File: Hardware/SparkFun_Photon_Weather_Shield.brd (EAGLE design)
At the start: 66 x 35.6 mm, 44 parts, among them U1 3.3V MIC5219, U2 HTU21D, U3 MPL3115A2LGA8

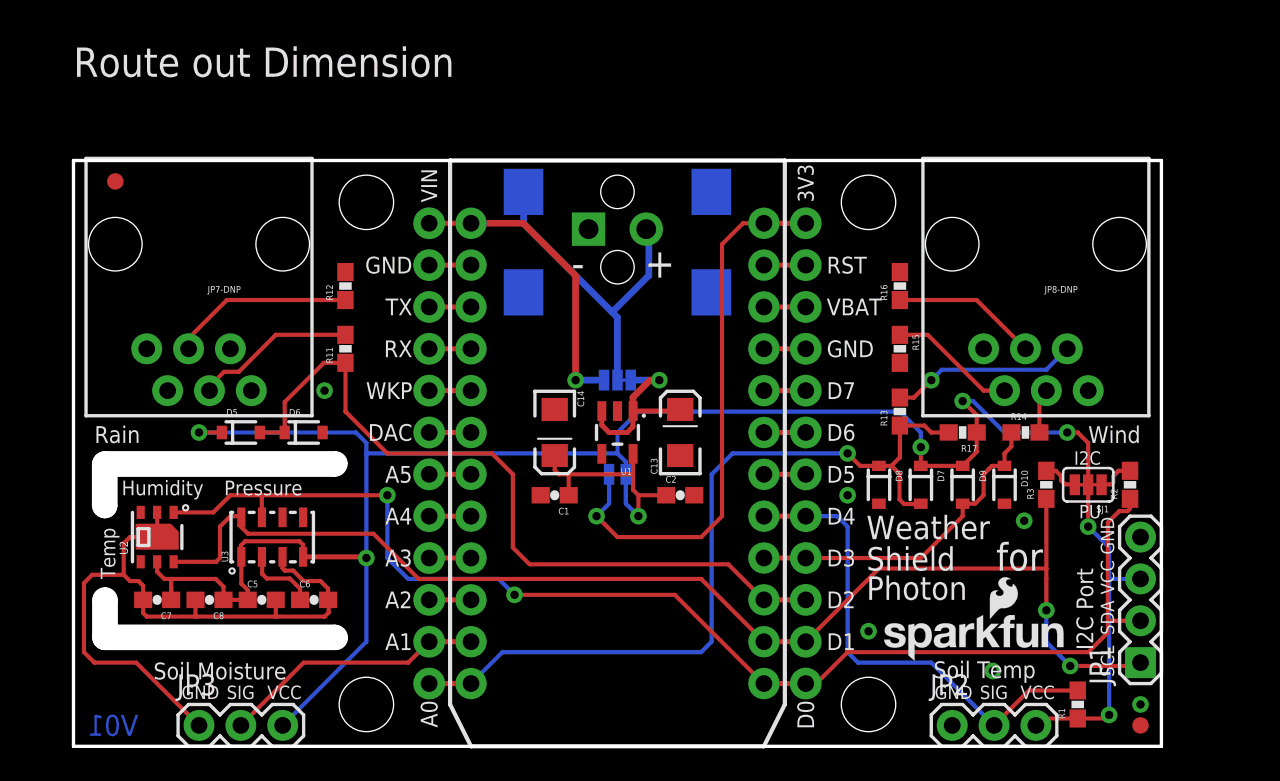
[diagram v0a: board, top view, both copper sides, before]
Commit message: Ready for Reds
Added USART port, changed soil moisture vcc to D5, minor silk and route
changes.
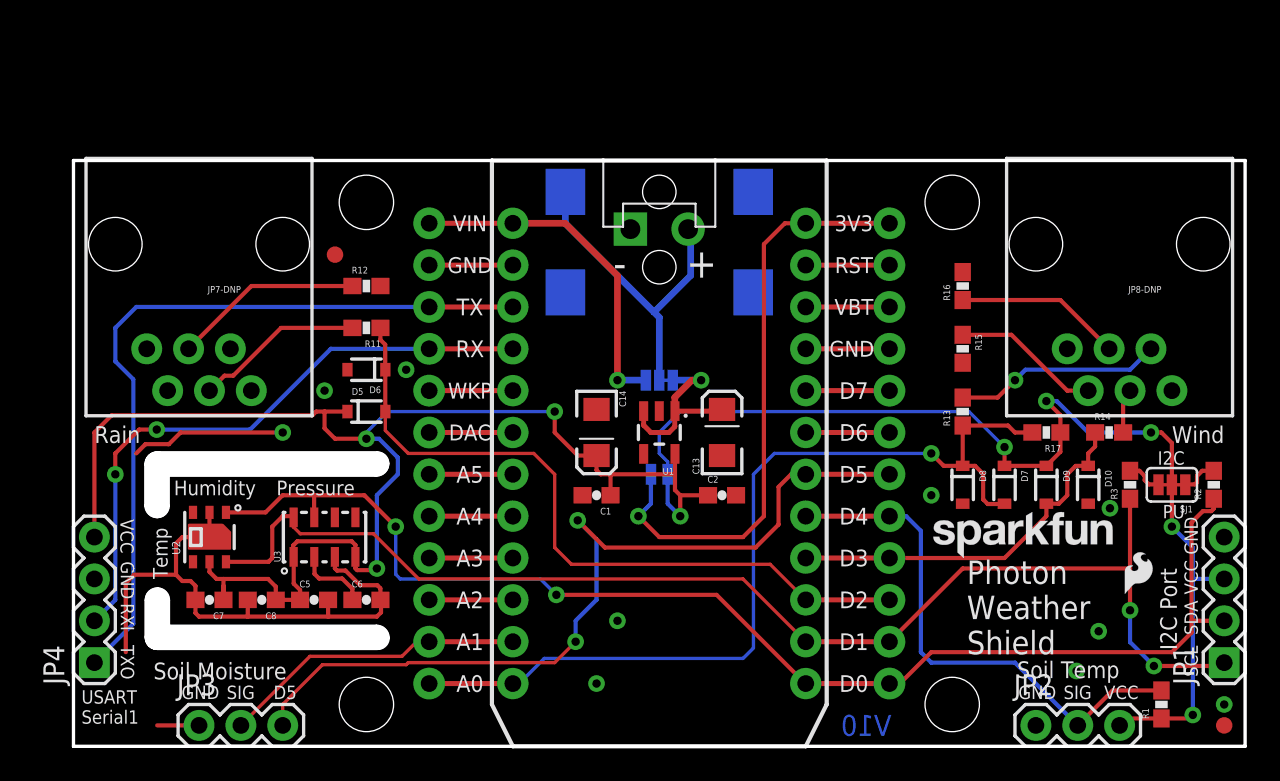
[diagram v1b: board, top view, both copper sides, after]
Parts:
- removed LOGO2: SFE_LOGO_NAME_FLAME.1_INCH, SparkFun-Aesthetics:SFE_LOGO_NAME_FLAME_.1
- added JP5: SPARK_PHOTONTEMPLATE_WIDE, template_temp:SPARK_PHOTON_TEMPLATE_WIDE
- added U$2: (no value), SparkFun-Aesthetics:SFE_LOGO_NAME_.1
- added U$3: (no value), SparkFun-Aesthetics:SFE_LOGO_FLAME_.1
- JP4: value SPARK_PHOTONTEMPLATE -> Serial1 Port; device template_temp:SPARK_PHOTON_TEMPLATE -> SparkFun-Connectors:1X04
- moved JP4 22.2 mm to (1.27, 5.08), turned to 90 degrees
- moved FID2 14.1 mm to (15.9, 29.8)
- moved D5 7.73 mm to (17.8, 20.3)
- moved D6 5.39 mm to (17.8, 22.9), turned to 180 degrees
- moved R1 5.08 mm to (66.0, 2.54)
- moved R14 5.08 mm to (62.9, 19.1)
- moved R3 5.08 mm to (64.1, 15.9)
- moved D10 5.08 mm to (61.6, 15.9)
- moved D7 5.08 mm to (56.5, 15.9)
- moved D8 5.08 mm to (54.0, 15.9)
- moved D9 5.08 mm to (59.1, 15.9)
- moved FID1 5.08 mm to (69.8, 1.27)
- moved JP1 5.08 mm to (69.8, 5.08)
- moved JP2 5.08 mm to (58.4, 1.27)
- moved JP8-DNP 5.08 mm to (63.5, 30.5)
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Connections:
- new net SOIL_MOIST_POWER: JP3.3, JP5.18, JP5.D5
- net 3.3V: now also JP4.4; no longer JP3.3
- net GND: now also JP4.3, JP5.2, JP5.21, JP5.GND@0, JP5.GND@2; no longer JP4.2, JP4.21, JP4.GND@0, JP4.GND@2
- net N$7: now also JP5.24, JP5.3V3; no longer JP4.24, JP4.3V3
- net PHOTON_VIN: now also JP5.1, JP5.VIN; no longer JP4.1, JP4.VIN
- net RAIN: now also JP5.15, JP5.D2; no longer JP4.15, JP4.D2
- net RXI: now also JP4.2, JP5.4, JP5.RX; no longer JP4.4, JP4.RX
- net SCL: now also JP5.14, JP5.D1; no longer JP4.14, JP4.D1
- net SDA: now also JP5.13, JP5.D0; no longer JP4.13, JP4.D0
- net SOIL_MOIST: now also JP5.11, JP5.A1; no longer JP4.11, JP4.A1
- net SOIL_TEMP: now also JP5.17, JP5.D4; no longer JP4.17, JP4.D4
- net TXO: now also JP4.1, JP5.3, JP5.TX; no longer JP4.3, JP4.TX
- net WDIR: now also JP5.12, JP5.A0; no longer JP4.12, JP4.A0
- net WSPEED: now also JP5.16, JP5.D3; no longer JP4.16, JP4.D3
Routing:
- net SOIL_MOIST_POWER: track 0.00 -> 46.7 mm, vias 0 -> 2
- net TXO: track 0.00 -> 41.3 mm
- net RXI: track 0.00 -> 32.4 mm, vias 0 -> 2
- net 3.3V: track 147.3 -> 153.7 mm, vias 8 -> 9
- net RAIN: track 43.7 -> 38.7 mm
- net WDIR: track 47.0 -> 50.9 mm
- net GND: track 43.3 -> 47.0 mm, vias 6 -> 10
- net SDA: track 75.8 -> 74.0 mm
- net N$13: track 8.85 -> 10.1 mm
- net N$2: track 11.4 -> 12.7 mm
- net N$12: track 7.75 -> 9.02 mm
- net SCL: track 73.1 -> 72.5 mm
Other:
- board size 66 x 35.6 mm -> 71.1 x 35.6 mm
- board text added: "D5"
- board text added: "Photon Weather Shield"
- board text added: "RXI"
- board text added: "Route Out"
- board text added: "TXO"
- board text added: "USART Serial1"
- board text added: "V10"
- board text removed: "Route out Dimension"
- board text removed: "Turn on Milling Layer (46)"
- board text removed: "V01"
- board text removed: "for"

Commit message: Ready for last QC Check
Most recent changes pushed to github include
-Locking Footprint added to Photon Template for selective soldering
-updating Photon template to wider version for selective solder
-breakout USART port
-changing power on Soil Moisture from Vcc to D5
-Minor route and silk changes.
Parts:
- removed JP5: SPARK_PHOTONTEMPLATE_WIDE, template_temp:SPARK_PHOTON_TEMPLATE_WIDE
- added JP9: PHOTON_TEMPLATE_WIDE_LOCKING, template_temp:SPARK_PHOTON_TEMPLATE_WIDE_LOCKING
- FRAME2: value (none) -> FRAME-LETTER
- moved FRAME2 3.81 mm to (7.62, -10.2)
- moved U$3 1.25 mm to (63.0, 10.0)
- moved U$2 1.17 mm to (50.5, 10.7)
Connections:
- net GND: now also JP9.2, JP9.21, JP9.GND@0, JP9.GND@2; no longer JP5.2, JP5.21, JP5.GND@0, JP5.GND@2
- net N$7: now also JP9.24, JP9.3V3; no longer JP5.24, JP5.3V3
- net PHOTON_VIN: now also JP9.1, JP9.VIN; no longer JP5.1, JP5.VIN
- net RAIN: now also JP9.15, JP9.D2; no longer JP5.15, JP5.D2
- net RXI: now also JP9.4, JP9.RX; no longer JP5.4, JP5.RX
- net SCL: now also JP9.14, JP9.D1; no longer JP5.14, JP5.D1
- net SDA: now also JP9.13, JP9.D0; no longer JP5.13, JP5.D0
- net SOIL_MOIST: now also JP9.11, JP9.A1; no longer JP5.11, JP5.A1
- net SOIL_MOIST_POWER: now also JP9.18, JP9.D5; no longer JP5.18, JP5.D5
- net SOIL_TEMP: now also JP9.17, JP9.D4; no longer JP5.17, JP5.D4
- net TXO: now also JP9.3, JP9.TX; no longer JP5.3, JP5.TX
- net WDIR: now also JP9.12, JP9.A0; no longer JP5.12, JP5.A0
- net WSPEED: now also JP9.16, JP9.D3; no longer JP5.16, JP5.D3

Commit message: Ready for Reds
Ready for Reds
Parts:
- LOGO2: value (none) -> SFE_LOGO_NAME.1_INCH
- moved U$3 0.38 mm to (63.0, 9.65)
- renumbered FRAME2 to FRAME1, JP7-DNP to JP7, JP8-DNP to JP8, U$2 to LOGO2
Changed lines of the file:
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@@
 <text x="65.8114" y="17.0942" size="0.8128" layer="21" font="vector" ratio="15">I2C</text>
 <text x="66.1162" y="13.843" size="0.8128" layer="21" font="vector" ratio="15">PU</text>
-<text x="39.751" y="11.557" size="1.778" layer="22" font="vector" ratio="15" rot="MR0">Photon</text>
+<text x="39.751" y="11.43" size="1.778" layer="22" font="vector" ratio="15" rot="MR0">Photon</text>
 <text x="40.386" y="8.89" size="1.778" layer="22" font="vector" ratio="15" rot="MR0">Weather</text>
 <text x="39.751" y="6.35" size="1.778" layer="22" font="vector" ratio="15" rot="MR0">Shield</text>
@@
 <text x="7.747" y="16.637" size="1.016" layer="51" font="vector" ratio="15">Route Out</text>
 <text x="7.747" y="6.096" size="1.016" layer="51" font="vector" ratio="15">Route Out</text>
+<dimension x1="17.78" y1="33.02" x2="53.34" y2="33.02" x3="35.56" y3="41.91" textsize="1.778" textratio="15" layer="47" dtype="horizontal" unit="inch"/>
+<dimension x1="17.78" y1="33.02" x2="17.78" y2="2.54" x3="-2.54" y3="17.78" textsize="1.778" textratio="15" layer="47" dtype="vertical" unit="inch"/>
 </plain>
 <attributes>
@@
 <attribute name="VALUE" value="10uF" x="31.75" y="19.05" size="1.778" layer="27" rot="R270" display="off"/>
 </element>
-<element name="FRAME2" library="SparkFun-Aesthetics" package="CREATIVE_COMMONS" value="FRAME-LETTER" x="7.62" y="-10.16"/>
-<element name="JP8-DNP" library="SparkFun-Connectors" package="RJ11-6" value="RJ11" x="63.5" y="30.48" rot="R180">
+<element name="JP8" library="SparkFun-Connectors" package="RJ11-6" value="RJ11" x="63.5" y="30.48" rot="R180">
 <attribute name="PROD_ID" value="CONN-08590" x="63.5" y="30.48" size="1.778" layer="27" rot="R180" display="off"/>
 <attribute name="VALUE" value="RJ11" x="63.5" y="30.48" size="1.778" layer="27" rot="R180" display="off"/>
 </element>
-<element name="JP7-DNP" library="SparkFun-Connectors" package="RJ11-6" value="RJ11" x="7.62" y="30.48" rot="R180">
+<element name="JP7" library="SparkFun-Connectors" package="RJ11-6" value="RJ11" x="7.62" y="30.48" rot="R180">
 <attribute name="PROD_ID" value="CONN-08590" x="7.62" y="30.48" size="1.778" layer="27" rot="R180" display="off"/>
 <attribute name="VALUE" value="RJ11" x="7.62" y="30.48" size="1.778" layer="27" rot="R180" display="off"/>
@@
 <element name="SJ3" library="SparkFun-Passives" package="PAD-JUMPER-2-NC_BY_TRACE_YES_SILK" value="" x="35.56" y="16.51" rot="MR180"/>
 <element name="JP4" library="SparkFun-Connectors" package="1X04" value="Serial1 Port" x="1.27" y="5.08" rot="R90"/>
-<element name="U$2" library="SparkFun-Aesthetics" package="SFE_LOGO_NAME_.1" value="" x="50.546" y="10.668"/>
-<element name="U$3" library="SparkFun-Aesthetics" package="SFE_LOGO_FLAME_.1" value="" x="62.992" y="10.033"/>
+<element name="U$3" library="SparkFun-Aesthetics" package="SFE_LOGO_FLAME_.1" value="" x="62.992" y="9.652"/>
 <element name="JP9" library="template_temp" package="SPARK_PHOTON_TEMPLATE_WIDE_LOCKING" value="PHOTON_TEMPLATE_WIDE_LOCKING" x="25.4" y="0"/>
+<element name="LOGO2" library="SparkFun-Aesthetics" package="SFE_LOGO_NAME_.1" value="SFE_LOGO_NAME.1_INCH" x="50.546" y="10.668"/>
+<element name="FRAME1" library="SparkFun-Aesthetics" package="CREATIVE_COMMONS" value="FRAME-LETTER" x="7.62" y="-10.16"/>
 </elements>
 <signals>
@@
 </signal>
 <signal name="RAIN2">
-<contactref element="JP7-DNP" pad="2"/>
+<contactref element="JP7" pad="2"/>
 </signal>
 <signal name="RAIN5">
-<contactref element="JP7-DNP" pad="5"/>
+<contactref element="JP7" pad="5"/>
 </signal>
 <signal name="N$2">
-<contactref element="JP8-DNP" pad="2"/>
+<contactref element="JP8" pad="2"/>
 <contactref element="R13" pad="2"/>
 <wire x1="65.405" y1="24.13" x2="64.135" y2="22.86" width="0.254" layer="16"/>
@@
 </signal>
 <signal name="N$1">
-<contactref element="JP8-DNP" pad="3"/>
+<contactref element="JP8" pad="3"/>
 <contactref element="R14" pad="2"/>
 <wire x1="63.715" y1="19.05" x2="63.715" y2="21.17" width="0.254" layer="1"/>
@@
 <signal name="N$4">
 <contactref element="R11" pad="2"/>
-<contactref element="JP7-DNP" pad="3"/>
+<contactref element="JP7" pad="3"/>
 <wire x1="9.7" y1="22.5" x2="9.165" y2="22.5" width="0.254" layer="1"/>
 <wire x1="9.165" y1="22.5" x2="8.255" y2="21.59" width="0.254" layer="1"/>
@@
 </signal>
 <signal name="N$11">
-<contactref element="JP7-DNP" pad="4"/>
+<contactref element="JP7" pad="4"/>
 <contactref element="R12" pad="1"/>
 <wire x1="10.795" y1="27.94" x2="6.985" y2="24.13" width="0.254" layer="1"/>
@@
 </signal>
 <signal name="N$12">
-<contactref element="JP8-DNP" pad="5"/>
+<contactref element="JP8" pad="5"/>
 <contactref element="R15" pad="1"/>
 <wire x1="61.595" y1="21.59" x2="60.325" y2="21.59" width="0.254" layer="1"/>
@@
 </signal>
 <signal name="N$13">
-<contactref element="JP8-DNP" pad="4"/>
+<contactref element="JP8" pad="4"/>
 <contactref element="R16" pad="1"/>
 <wire x1="62.865" y1="24.13" x2="59.905" y2="27.09" width="0.254" layer="1"/>
